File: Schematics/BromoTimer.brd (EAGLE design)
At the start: 101.6 x 80 mm, 29 parts, among them IC1 PIC16F687, IC2 7805TV, K1 G2R2A, K2 G2R2A, Q1 BC548B, Q2 BC548B, Q3 BC548B, X1 AC_IN, X4 22-23-2031, X5 AC_OUT

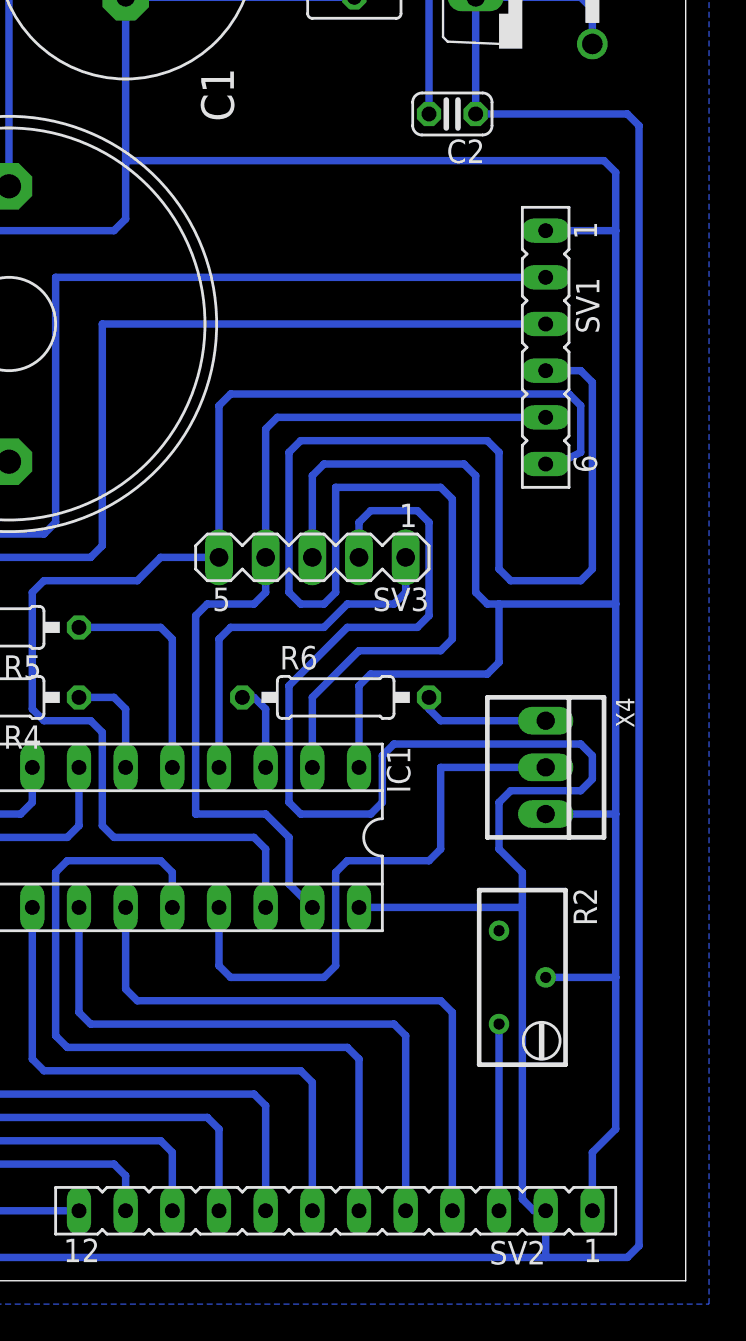
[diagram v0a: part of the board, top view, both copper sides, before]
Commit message: Add support for lid state sensor
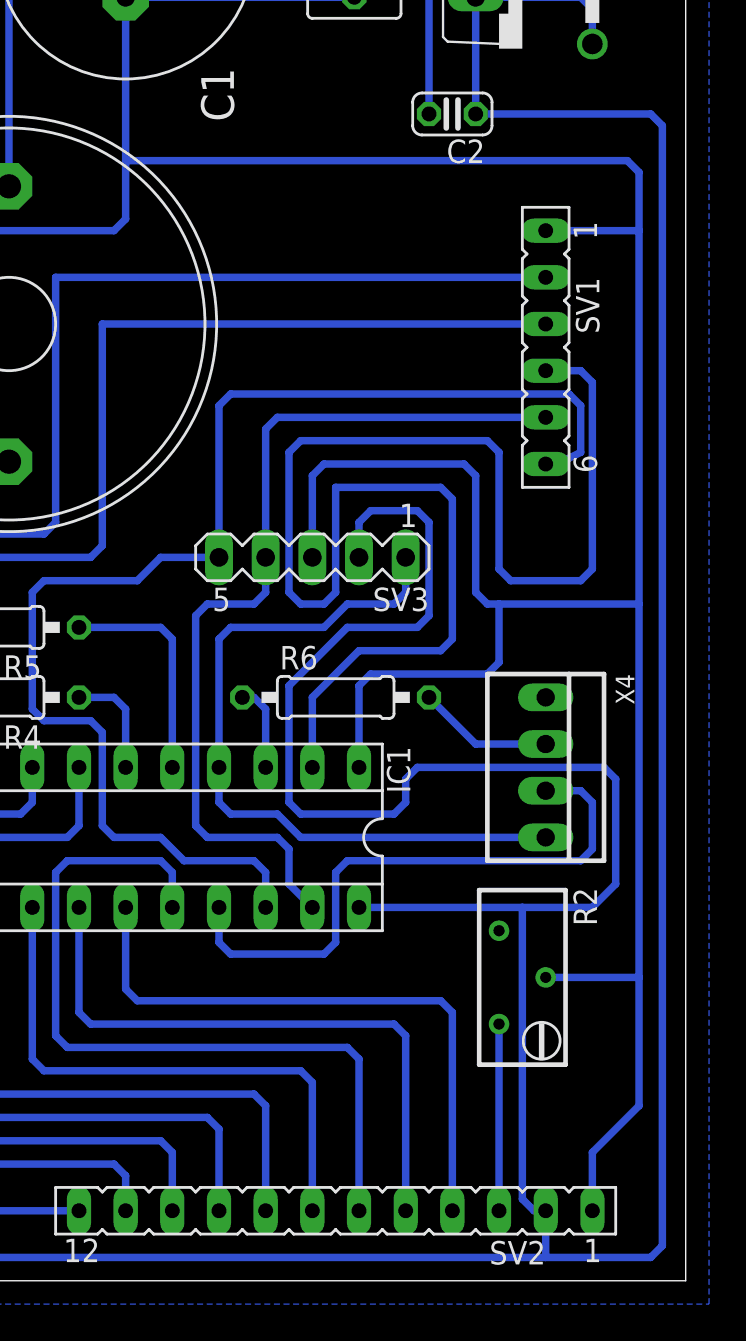
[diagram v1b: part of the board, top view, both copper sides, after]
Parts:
- X4: value 22-23-2031 -> 22-23-2041; device con-molex:22-23-2031 -> con-molex:22-23-2041
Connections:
- net GND: now also X4.1; no longer X4.3
- net N$13: now also X4.3; no longer X4.2
- net N$15: now also X4.4
- net N$21: now also X4.2; no longer X4.1
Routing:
- net N$15: track 20.1 -> 40.6 mm
- net GND: track 296.7 -> 298.5 mm
- net N$13: track 31.5 -> 32.4 mm
- net B: track 72.4 -> 71.6 mm
- net +5V: track 274.4 -> 275.2 mm

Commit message: Small changes to PCB layout.
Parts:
- moved D3 1.27 mm to (96.5, 71.1)
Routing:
- net GND: track 298.5 -> 0.00 mm
- net +5V: track 275.2 -> 286.4 mm
- net SW: track 80.3 -> 74.8 mm
- net V+: track 66.3 -> 65.1 mm
- net N$21: track 7.40 -> 8.52 mm
- net B: track 71.6 -> 72.6 mm

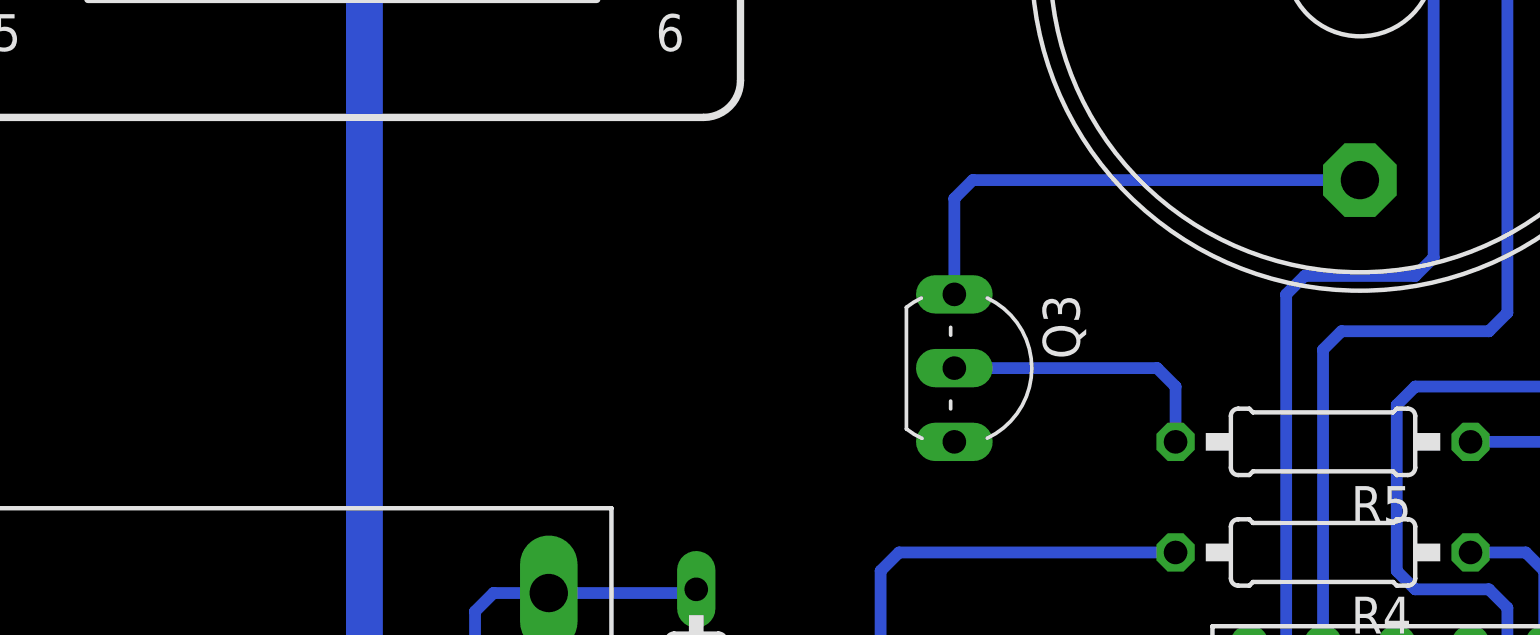
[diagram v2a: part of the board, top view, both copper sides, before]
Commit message: Add board name & version in layout.
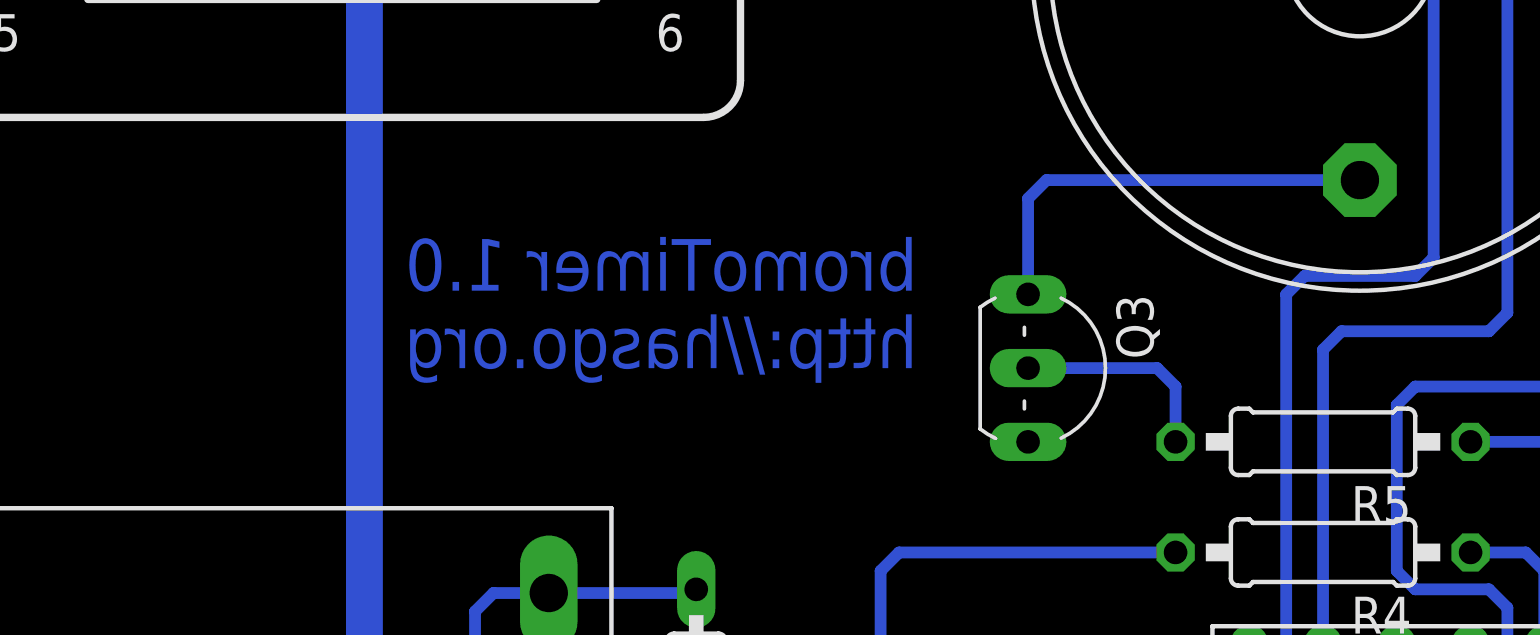
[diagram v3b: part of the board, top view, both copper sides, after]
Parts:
- moved Q3 2.54 mm to (54.6, 38.1)
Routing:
- net N$18: track 9.79 -> 7.25 mm
- net N$19: track 17.5 -> 15.0 mm
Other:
- board text added: "bromoTimer 1.0 http://hasgo.org"
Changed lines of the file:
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@@
 <wire x1="101.6" y1="80.01" x2="0" y2="80.01" width="0" layer="20"/>
 <wire x1="0" y1="80.01" x2="0" y2="0" width="0" layer="20"/>
+<text x="49.53" y="38.1" size="1.778" layer="16" rot="MR0">bromoTimer 1.0
+http://hasgo.org</text>
 </plain>
 <attributes>
@@
 </element>
 <element name="D3" library="diode" package="DO41-10" value="1N4004" x="96.52" y="71.12" rot="R270"/>
-<element name="Q3" library="transistor-npn" package="TO92-EBC" value="BC548B" x="52.07" y="38.1" rot="R270"/>
+<element name="Q3" library="transistor-npn" package="TO92-EBC" value="BC548B" x="54.61" y="38.1" rot="R270"/>
 <element name="R5" library="rcl" package="0207/10" value="" x="63.5" y="35.56" rot="R180"/>
 <element name="X4" library="con-molex" package="22-23-2041" value="22-23-2041" x="93.98" y="27.94" rot="R270">
@@
 <contactref element="Q3" pad="B"/>
 <contactref element="R5" pad="2"/>
-<wire x1="50.8" y1="38.1" x2="57.785" y2="38.1" width="0.4064" layer="16"/>
+<wire x1="53.34" y1="38.1" x2="57.785" y2="38.1" width="0.4064" layer="16"/>
 <wire x1="57.785" y1="38.1" x2="58.42" y2="37.465" width="0.4064" layer="16"/>
 <wire x1="58.42" y1="37.465" x2="58.42" y2="35.56" width="0.4064" layer="16"/>
@@
 <contactref element="Q3" pad="C"/>
 <contactref element="SG1" pad="-"/>
-<wire x1="50.8" y1="40.64" x2="50.8" y2="43.942" width="0.4064" layer="16"/>
-<wire x1="50.8" y1="43.942" x2="51.435" y2="44.577" width="0.4064" layer="16"/>
-<wire x1="51.435" y1="44.577" x2="64.77" y2="44.577" width="0.4064" layer="16"/>
+<wire x1="53.34" y1="40.64" x2="53.34" y2="43.942" width="0.4064" layer="16"/>
+<wire x1="53.34" y1="43.942" x2="53.975" y2="44.577" width="0.4064" layer="16"/>
+<wire x1="53.975" y1="44.577" x2="64.77" y2="44.577" width="0.4064" layer="16"/>
 </signal>
 <signal name="N$20">
@@
 </board>
 </drawing>
+<compatibility>
+<note version="6.3" minversion="6.2.2" severity="warning">
+Since Version 6.2.2 text objects can contain more than one line,
+which will not be processed correctly with this version.
+</note>
+</compatibility>
 </eagle>
